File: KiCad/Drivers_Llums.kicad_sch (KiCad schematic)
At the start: 0 parts

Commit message: Nada
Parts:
- added F1: Fuse, symbol Device:Fuse
- added LA1: Lamp12V, symbol Device:Lamp
- added Q1: AO3400A, Package_TO_SOT_SMD:SOT-23, symbol Transistor_FET:AO3400A
- added R1: 10k, symbol Device:R_US
- added R2: 100, symbol Device:R_US
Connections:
- new net: Q1.1 (G), R1.1, R2.2
- new net: F1.1, LA1.2 (+)
- new net: LA1.1 (-), Q1.3 (D)
- new net DRL_CTRL: R2.1
- new net GND: Q1.2 (S), R1.2
- new net Vbat: F1.2

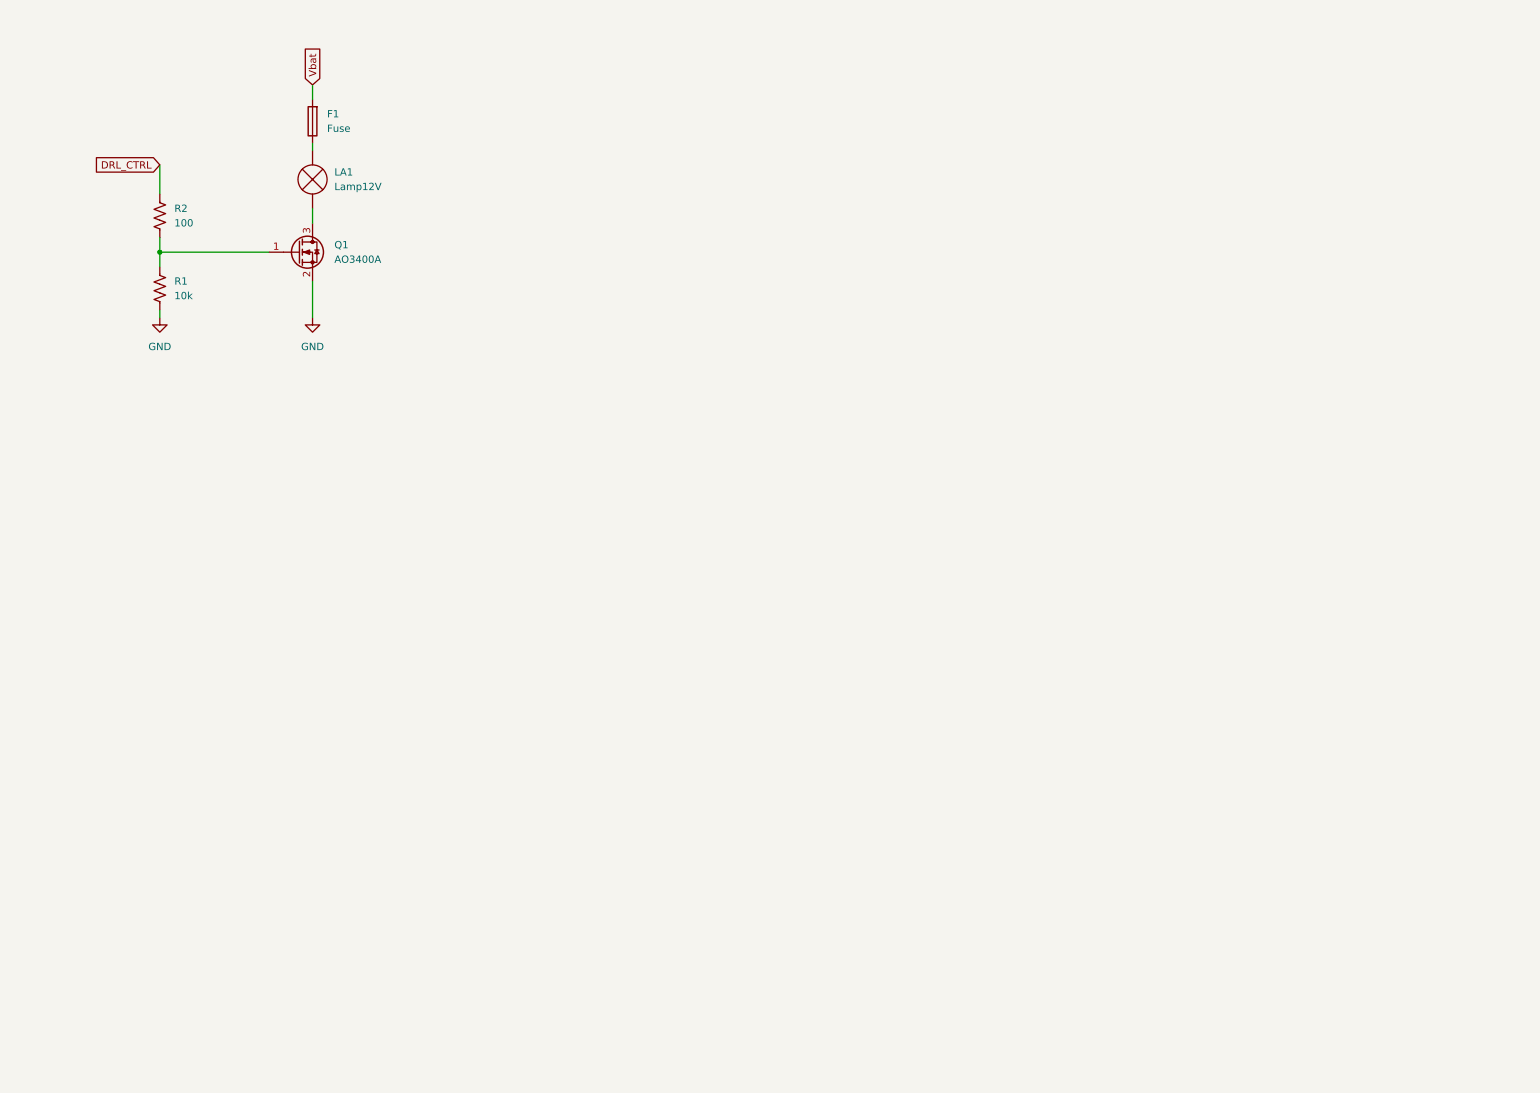
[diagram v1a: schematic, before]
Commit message: Driver llums fet
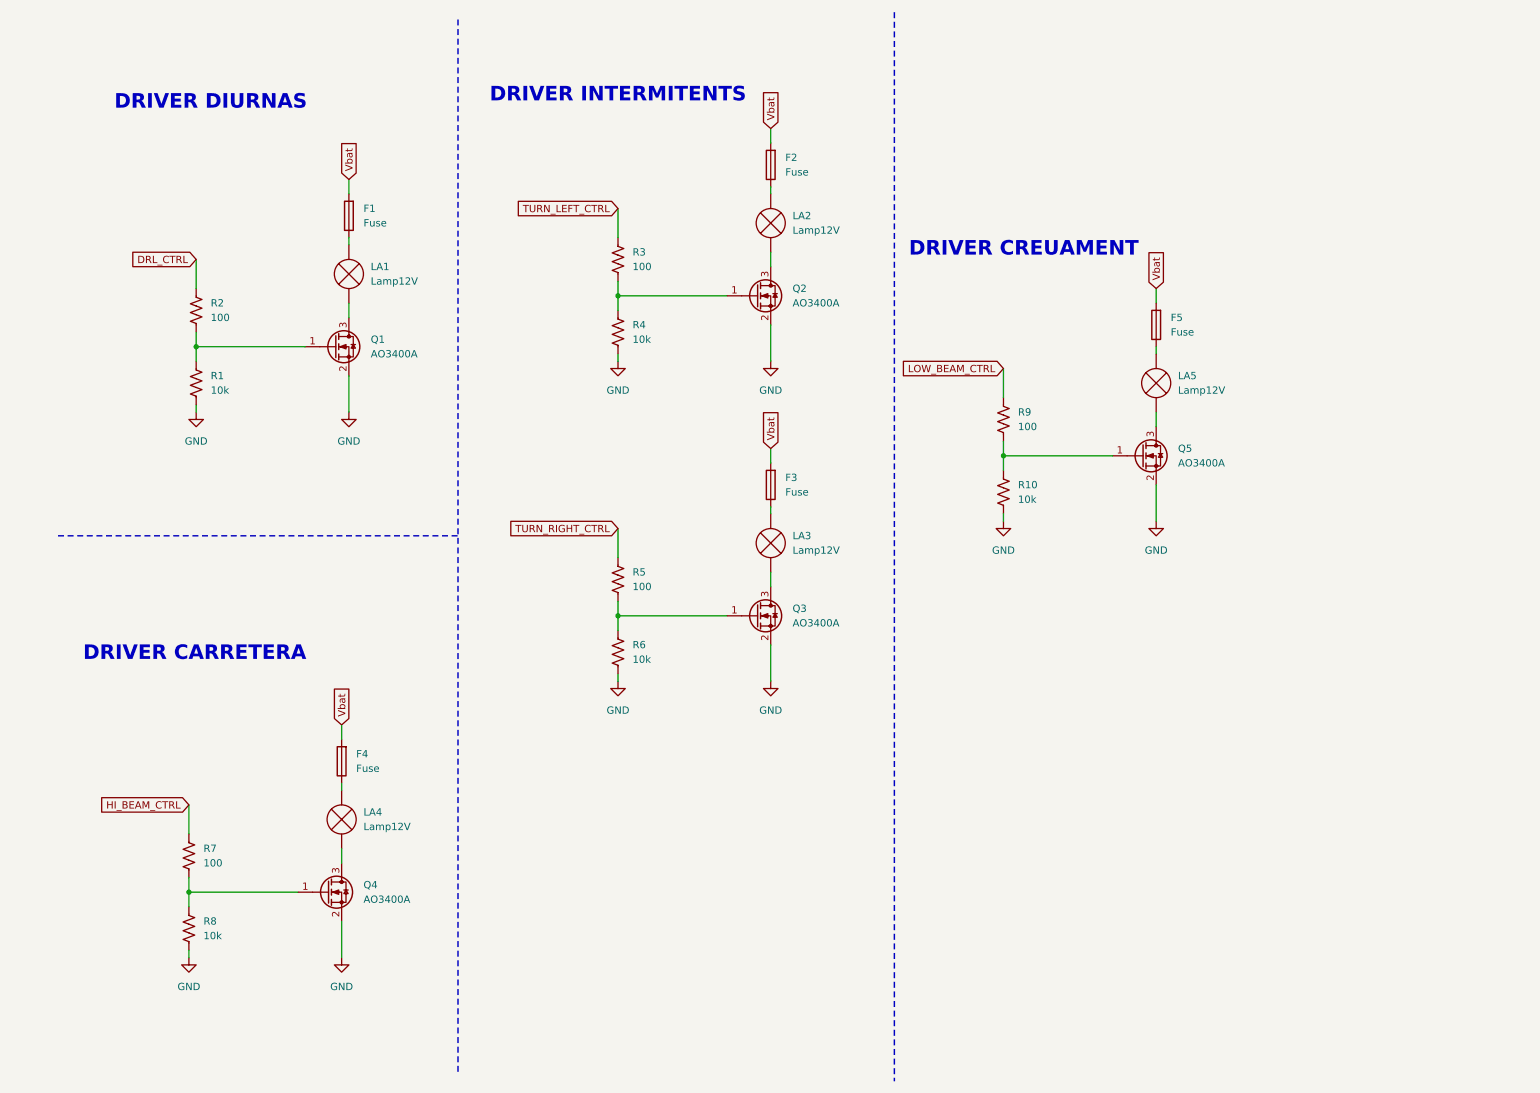
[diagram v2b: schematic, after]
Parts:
- added F2, F3, F4, F5: Fuse, symbol Device:Fuse
- added LA2, LA3, LA4, LA5: Lamp12V, symbol Device:Lamp
- added Q2, Q3, Q4, Q5: AO3400A, Package_TO_SOT_SMD:SOT-23, symbol Transistor_FET:AO3400A
- added R10, R4, R6, R8: 10k, symbol Device:R_US
- added R3, R5, R7, R9: 100, symbol Device:R_US
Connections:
- net GND: now also Q2.2 (S), Q3.2 (S), Q4.2 (S), Q5.2 (S), R10.2, R4.2, R6.2, R8.2
- net Vbat: now also F2.2, F3.2, F4.2, F5.2
- new net: F2.1, LA2.2 (+)
- new net: F4.1, LA4.2 (+)
- new net: Q3.1 (G), R5.2, R6.1
- new net: LA3.1 (-), Q3.3 (D)
- new net: LA5.1 (-), Q5.3 (D)
- new net: F5.1, LA5.2 (+)
- new net: Q2.1 (G), R3.2, R4.1
- new net: F3.1, LA3.2 (+)
- new net: Q5.1 (G), R10.1, R9.2
- new net: LA4.1 (-), Q4.3 (D)
- new net: LA2.1 (-), Q2.3 (D)
- new net: Q4.1 (G), R7.2, R8.1
- new net HI_BEAM_CTRL: R7.1
- new net LOW_BEAM_CTRL: R9.1
- new net TURN_LEFT_CTRL: R3.1
- new net TURN_RIGHT_CTRL: R5.1
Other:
- note added: "DRIVER CARRETERA"
- note added: "DRIVER CREUAMENT"
- note added: "DRIVER DIURNAS"
- note added: "DRIVER INTERMITENTS"
- moved on the sheet: F1, LA1, Q1, R1, R2

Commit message: acabar can, estil y micro biel
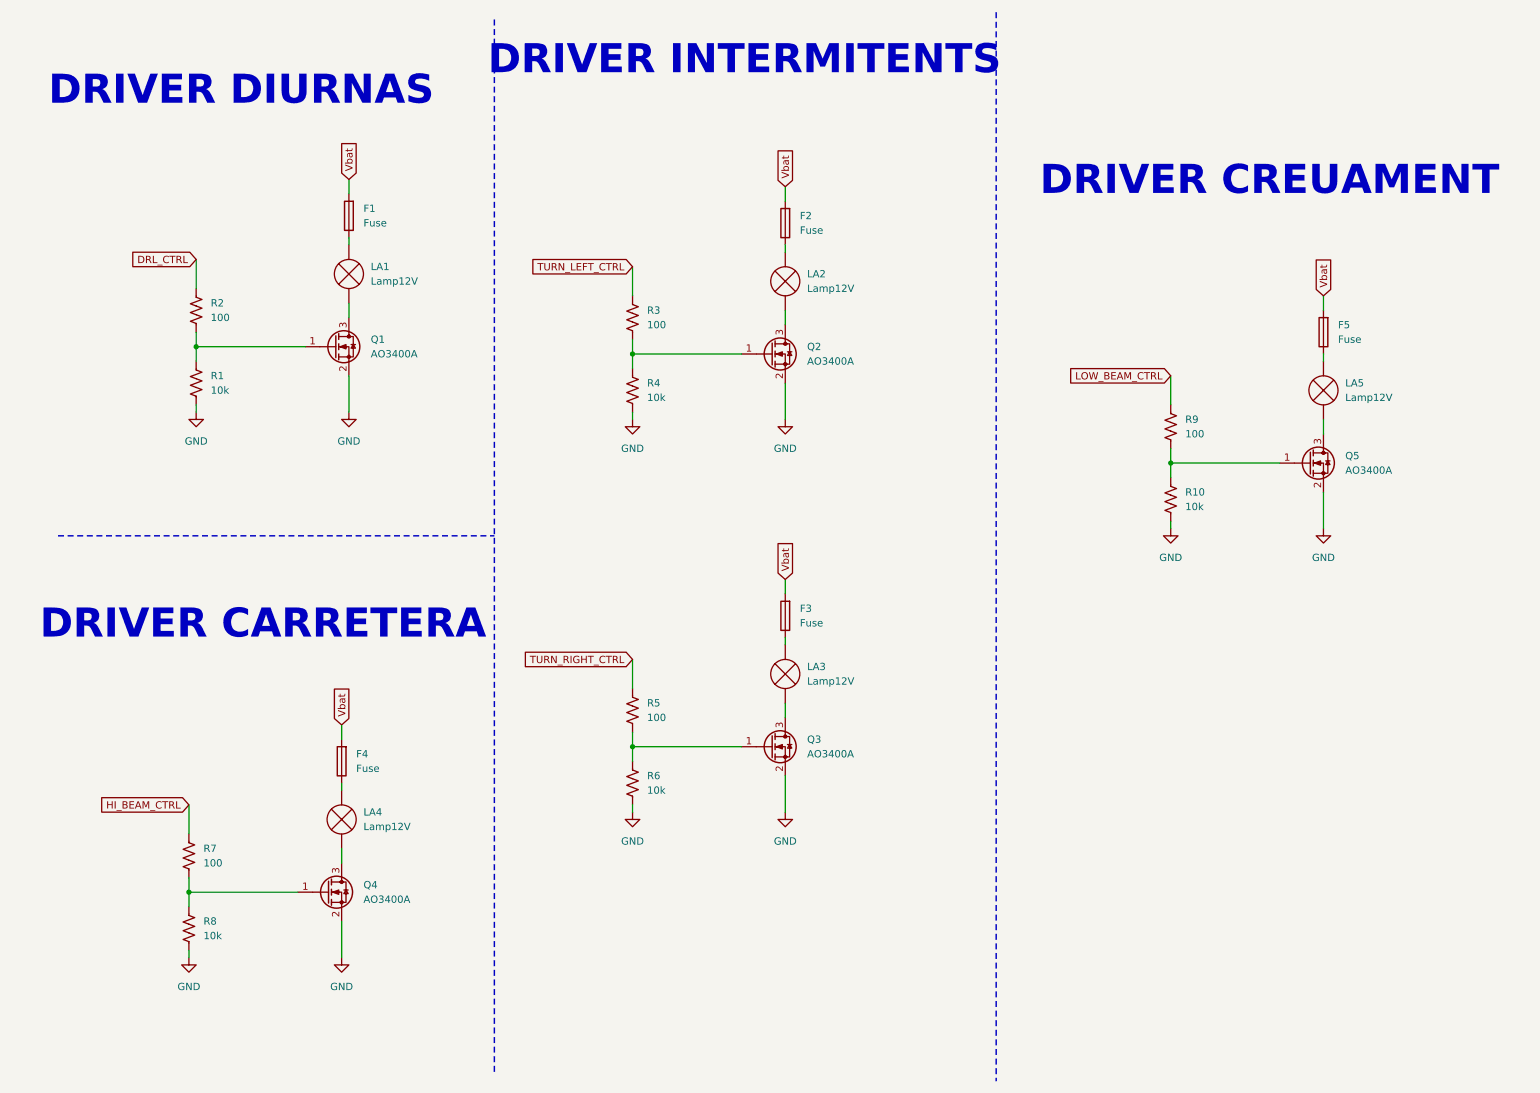
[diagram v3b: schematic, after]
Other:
- moved on the sheet: F2, F3, F5, LA2, LA3, LA5, Q2, Q3, Q5, R10, R3, R4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
